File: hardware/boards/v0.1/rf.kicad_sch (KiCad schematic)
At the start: 11 parts, among them U22 nRF, Y2 32.768kHz

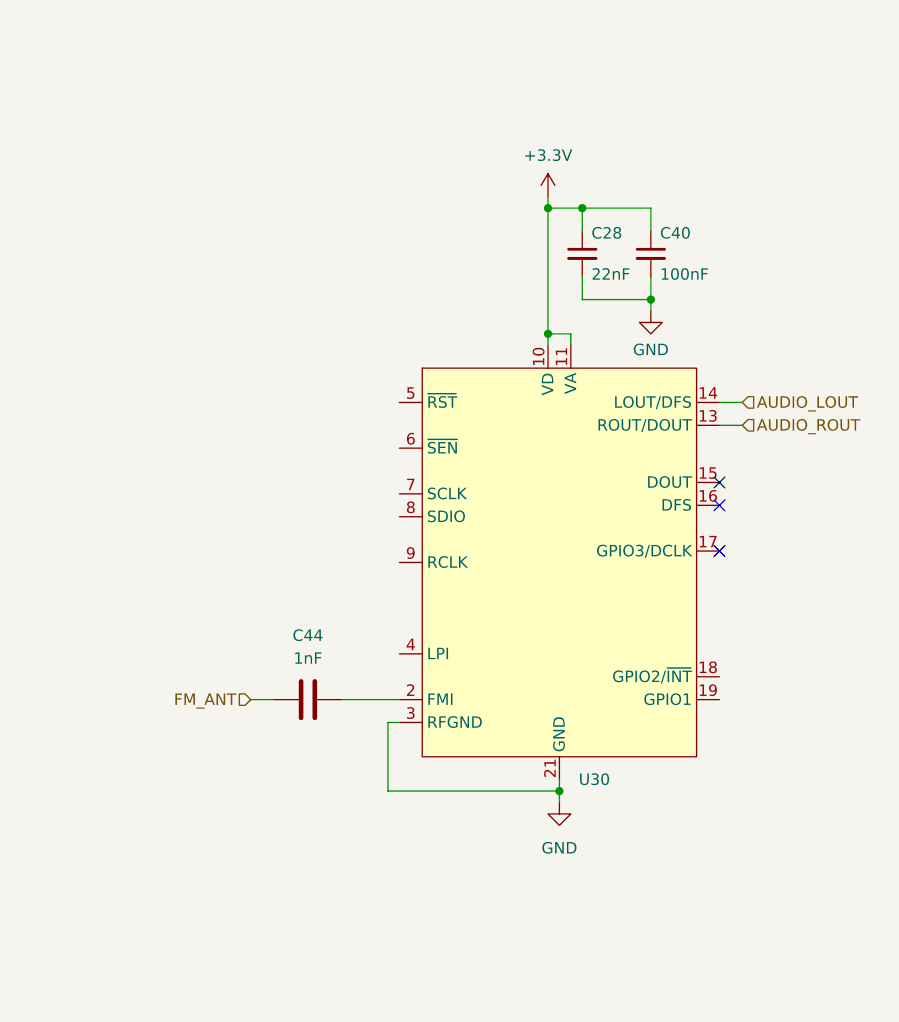
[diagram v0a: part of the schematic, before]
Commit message: feat: FM receiver routing
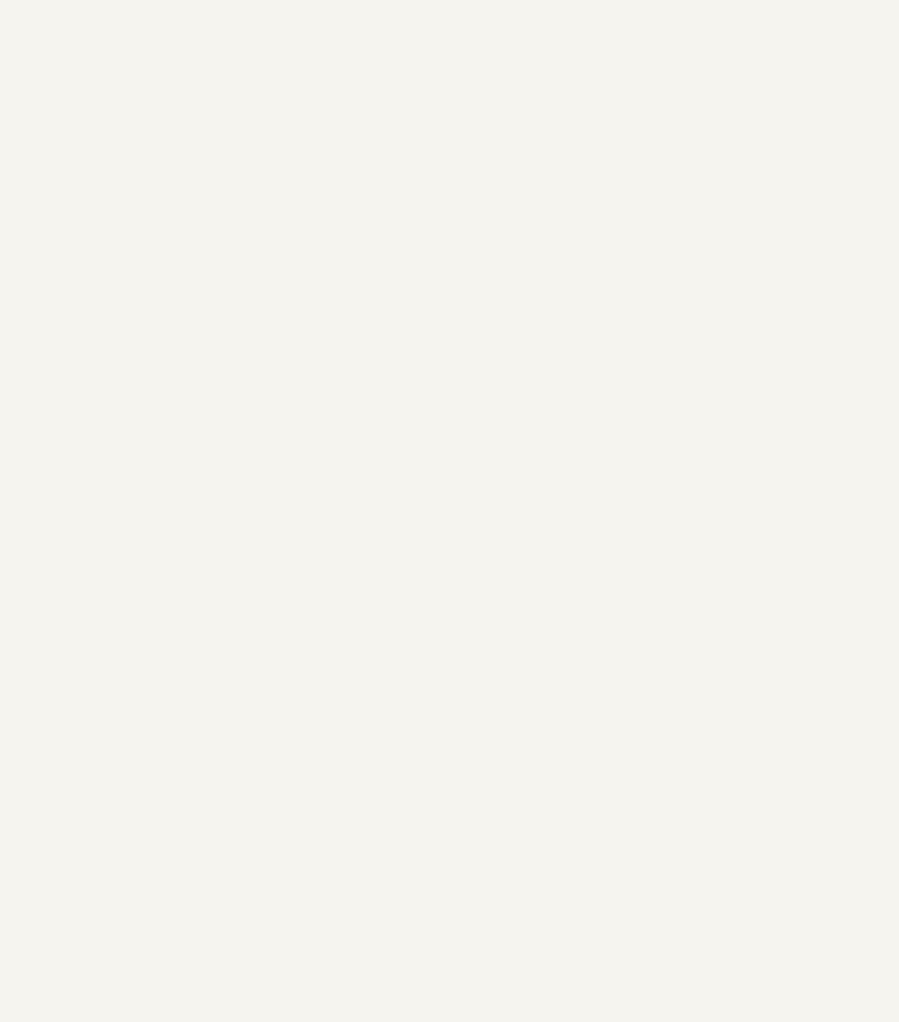
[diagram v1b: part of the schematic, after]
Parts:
- removed C28: 22nF, symbol Device:C_Small
- removed C40: 100nF, symbol Device:C_Small
- removed C44: 1nF, symbol Device:C
- removed U30: ~, pocket_synth:SI4704-D60-GMR, symbol pocket_synth:SI4704-D60-GM
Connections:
- no-connect marks 9 -> 6

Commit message: feat: start adding FM receiver
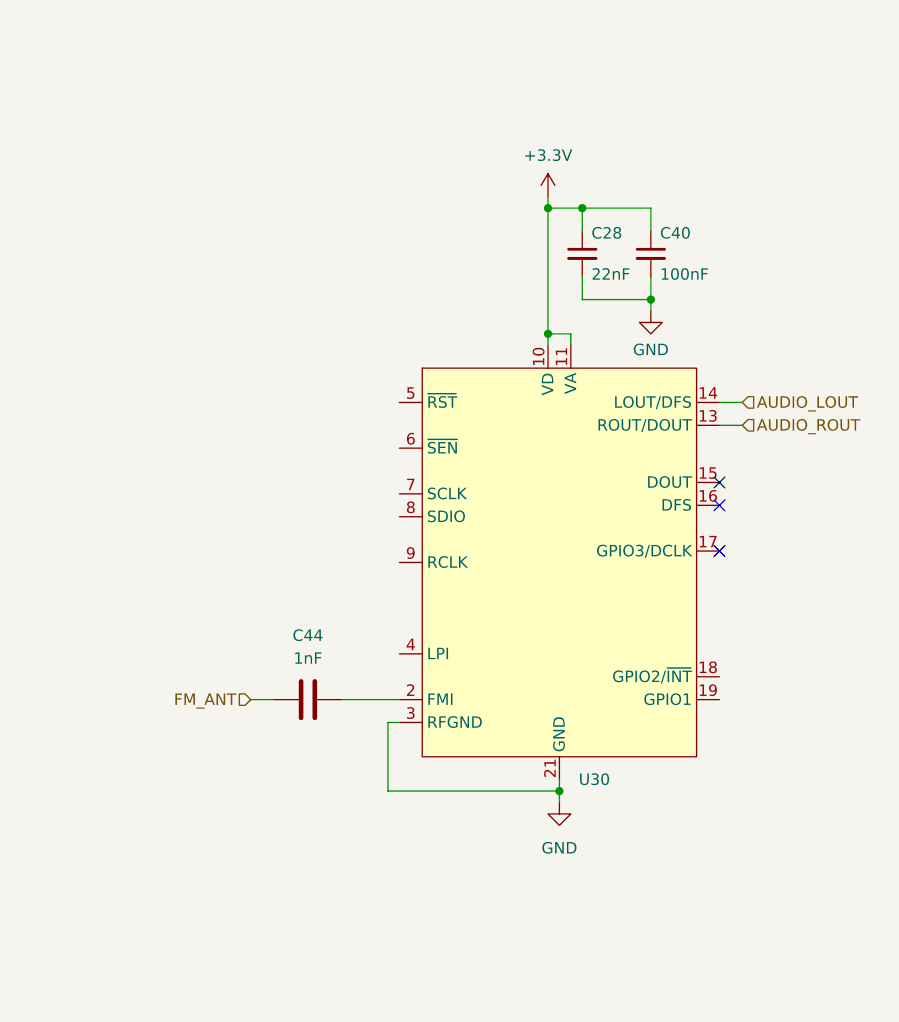
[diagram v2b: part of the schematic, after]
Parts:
- added C28: 22nF, symbol Device:C_Small
- added C40: 100nF, symbol Device:C_Small
- added C44: 1nF, symbol Device:C
- added U30: ~, pocket_synth:SI4704-D60-GMR, symbol pocket_synth:SI4704-D60-GM
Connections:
- net +3.3V: now also C28.1, C40.1, U30.10 (VD), U30.11 (VA)
- net GND: now also C28.2, C40.2, U30.12 (GND), U30.21 (GND), U30.3 (RFGND)
- new net: C44.2, U30.2 (FMI)
- new net AUDIO_LOUT: U30.14 (LOUT/DFS)
- new net AUDIO_ROUT: U30.13 (ROUT/DOUT)
- new net FM_ANT: C44.1
- no-connect marks 6 -> 9
